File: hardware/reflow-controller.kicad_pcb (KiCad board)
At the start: 2 copper layers, 39.4 x 30.5 mm, 27 parts, among them J1 USB_B_Mini, J2 Conn_01x02, J3 Conn_02x03_Odd_Even, J4 Conn_01x02, J5 Conn_01x04, Q1 BC817, U1 MAX31855KASA, U2 AP2127K-3.3, U3 ATmega8U2-AU, Y1 8MHz

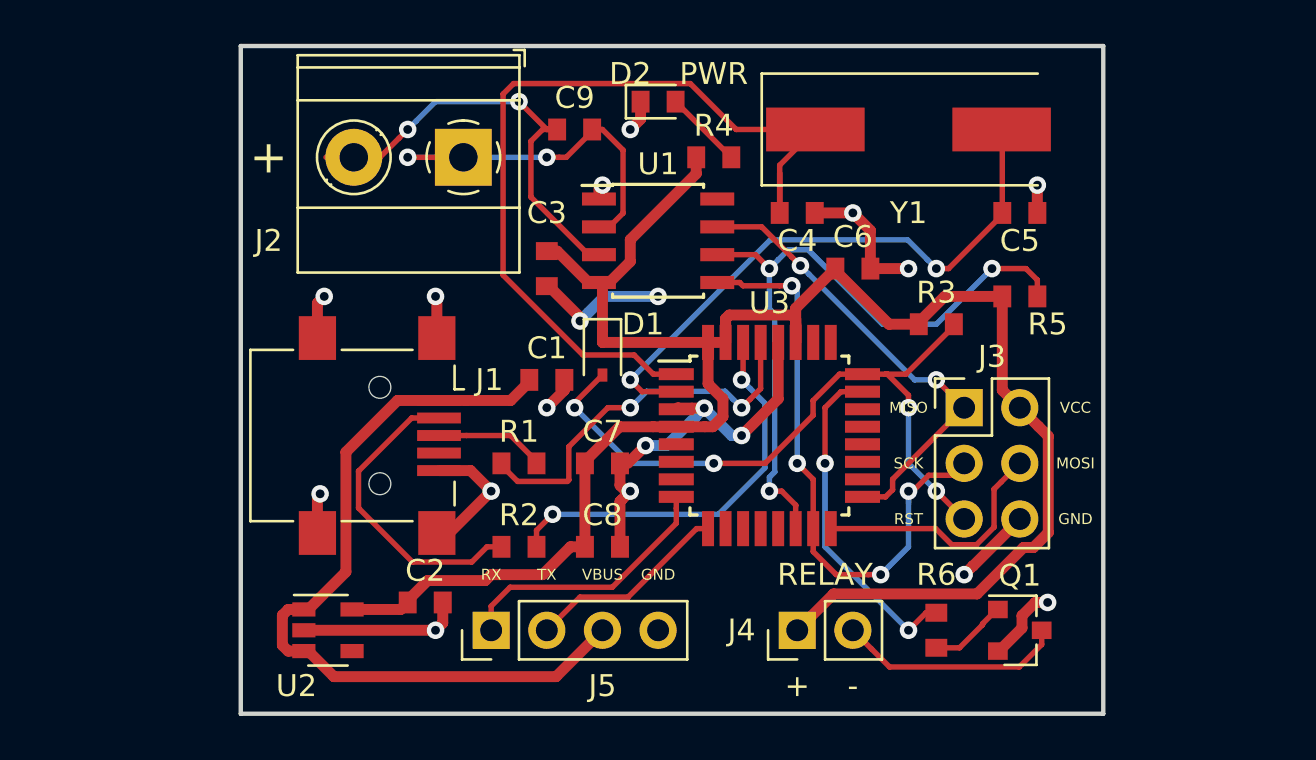
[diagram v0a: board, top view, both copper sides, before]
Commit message: Fixed power supply when programmed by ISP, added mounting holes, replaced mini USB connector with micro connector.
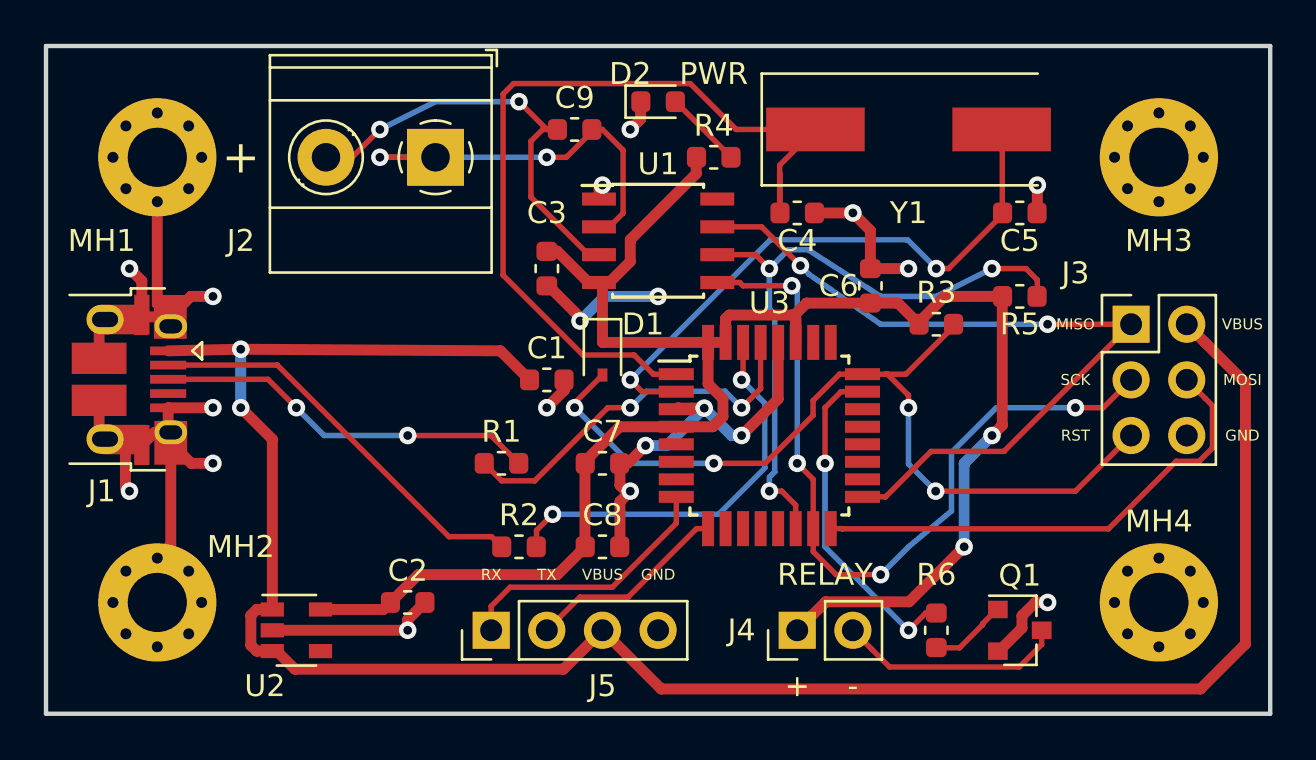
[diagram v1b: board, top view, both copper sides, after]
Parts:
- added MH1: MountingHole_Pad, MountingHole:MountingHole_2.7mm_M2.5_Pad_Via, F.Cu at (161.3, 52.1)
- added MH2: MountingHole_Pad, MountingHole:MountingHole_2.7mm_M2.5_Pad_Via, F.Cu at (161.3, 72.4)
- added MH3: MountingHole_Pad, MountingHole:MountingHole_2.7mm_M2.5_Pad_Via, F.Cu at (207.0, 52.1)
- added MH4: MountingHole_Pad, MountingHole:MountingHole_2.7mm_M2.5_Pad_Via, F.Cu at (207.0, 72.4)
- J1: value USB_B_Mini -> USB_B_Micro; footprint Connector_USB:USB_Mini-B_Lumberg_2486_01_Horizontal -> Connector_USB:USB_Micro-B_Amphenol_10103594-0001LF_Horizontal
- moved J1 11.7 mm to (160.0, 62.2)
- moved J3 8.52 mm to (205.7, 59.7)
- moved U2 1.44 mm to (167.6, 73.7)
- moved J2 1.27 mm to (174.0, 52.1)
- moved C6 1.12 mm to (193.8, 57.9), turned to 90 degrees
- moved C2 0.80 mm to (172.7, 72.4)
- moved R1 0.80 mm to (177.0, 66.0)
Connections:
- J3 pad 2: VCC -> /VBUS
- U2 pad 4: Net-(U2-Pad4) -> (no net)
- U3 pad 10: Net-(U3-Pad10) -> (no net)
- U3 pad 11: Net-(U3-Pad11) -> (no net)
- U3 pad 12: Net-(U3-Pad12) -> (no net)
- U3 pad 13: Net-(U3-Pad13) -> (no net)
- U3 pad 18: Net-(U3-Pad18) -> (no net)
- U3 pad 19: Net-(U3-Pad19) -> (no net)
- U3 pad 20: Net-(U3-Pad20) -> (no net)
- U3 pad 21: Net-(U3-Pad21) -> (no net)
- U3 pad 22: Net-(U3-Pad22) -> (no net)
- U3 pad 25: Net-(U3-Pad25) -> (no net)
- U3 pad 26: Net-(U3-Pad26) -> (no net)
- U3 pad 5: Net-(U3-Pad5) -> (no net)
- U3 pad 6: Net-(U3-Pad6) -> (no net)
- U3 pad 7: Net-(U3-Pad7) -> (no net)
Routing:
- net /VBUS: track 36.6 -> 96.2 mm, vias 0 -> 2
- net GND: track 62.4 -> 84.1 mm, vias 24 -> 19
- net /MISO: track 21.3 -> 36.0 mm
- net Net-(J1-Pad3): track 5.03 -> 17.6 mm, vias 0 -> 2
- net /MOSI: track 11.5 -> 22.6 mm
- net /SCK: track 28.2 -> 36.8 mm
- net /RST: track 31.7 -> 39.8 mm
- net Net-(J1-Pad2): track 14.2 -> 18.7 mm
- net VCC: track 91.9 -> 88.2 mm, vias 0 -> 2
- net Net-(C9-Pad2): track 16.3 -> 18.8 mm
- net /SS: track 32.0 -> 30.5 mm
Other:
- board size 39.4 x 30.5 mm -> 55.9 x 30.5 mm
- board text removed: "VCC"

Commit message: Fixed minimum values for solder mask clearance and width.
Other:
- rule pad_to_mask_clearance: 0.2 -> 0.0762
- rule solder_mask_min_width: 0.25 -> 0.1016
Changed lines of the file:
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@@
-(kicad_pcb (version 20171130) (host pcbnew 6.0.0-rc1-unknown-6a6d580~84~ubuntu18.04.1)
+(kicad_pcb (version 20171130) (host pcbnew 6.0.0-rc1-unknown-c4cd81a~84~ubuntu18.04.1)
   (general
     (thickness 1.6)
@@
     (pad_size 1.524 1.524)
     (pad_drill 0.762)
-    (pad_to_mask_clearance 0.2)
-    (solder_mask_min_width 0.25)
+    (pad_to_mask_clearance 0.0762)
+    (solder_mask_min_width 0.1016)
     (aux_axis_origin 0 0)
     (visible_elements FFFFFF7F)

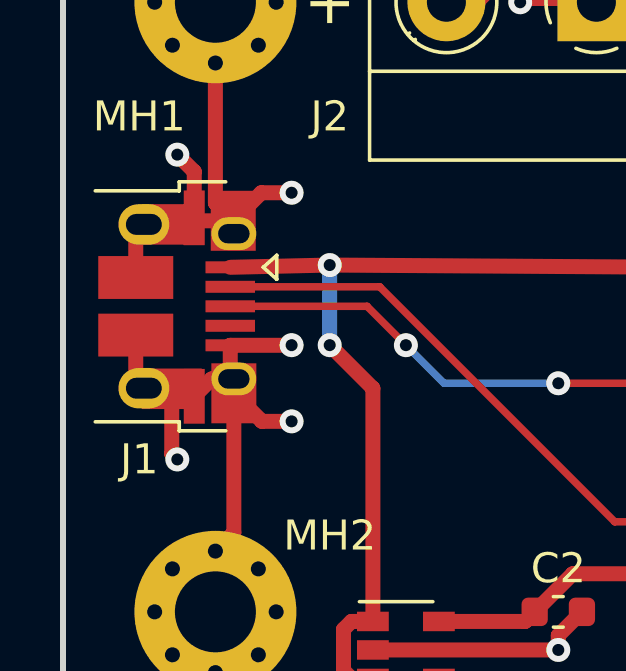
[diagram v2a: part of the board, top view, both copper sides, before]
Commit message: Adjusted solder mask relief and rewrote PC code in C++.
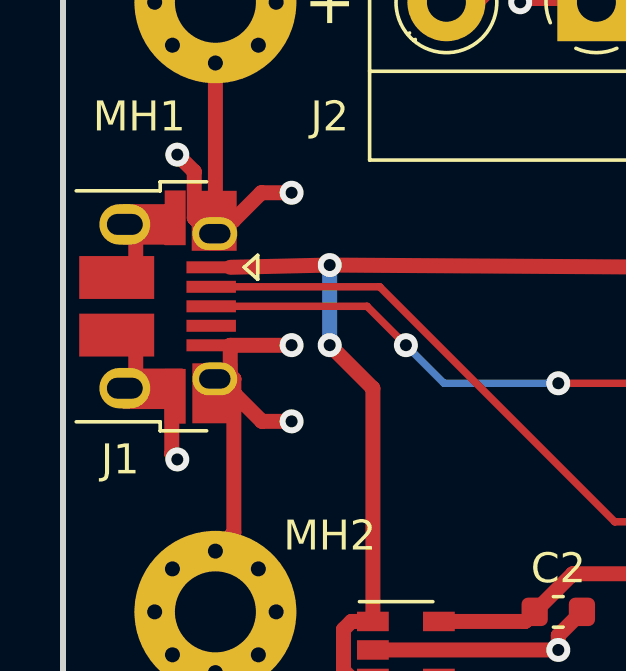
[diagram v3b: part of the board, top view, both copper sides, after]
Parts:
- moved J1 0.64 mm to (159.4, 62.2)
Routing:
- net GND: track 84.1 -> 83.3 mm
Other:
- rule pad_to_mask_clearance: 0.0762 -> 0.0508
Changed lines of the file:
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@@
-(kicad_pcb (version 20171130) (host pcbnew 6.0.0-rc1-unknown-c4cd81a~84~ubuntu18.04.1)
+(kicad_pcb (version 20171130) (host pcbnew 6.0.0-rc1-unknown-be0935b~84~ubuntu18.04.1)
   (general
     (thickness 1.6)
     (drawings 19)
-    (tracks 369)
+    (tracks 368)
     (zones 0)
     (modules 31)
@@
     (pad_size 1.524 1.524)
     (pad_drill 0.762)
-    (pad_to_mask_clearance 0.0762)
+    (pad_to_mask_clearance 0.0508)
     (solder_mask_min_width 0.1016)
     (aux_axis_origin 0 0)
@@
   )
   (module Connector_USB:USB_Micro-B_Amphenol_10103594-0001LF_Horizontal (layer F.Cu)
-    (at 160.02 62.23 270)
+    (at 159.385 62.23 270)
     (descr "Micro USB Type B 10103594-0001LF, http://cdn.amphenol-icc.com/media/wysiwyg/files/drawing/10103594.pdf")
     (tags "USB USB_B USB_micro USB_OTG")
@@
   (segment (start 161.785 64.505) (end 161.905 64.625) (width 0.5) (layer F.Cu) (net 1) (status 30))
   (segment (start 161.785 63.505) (end 161.785 64.505) (width 0.5) (layer F.Cu) (net 1) (status 30))
-  (segment (start 161.165 64.625) (end 160.585 65.205) (width 0.5) (layer F.Cu) (net 1) (status 30))
   (segment (start 161.905 64.625) (end 161.165 64.625) (width 0.5) (layer F.Cu) (net 1) (status 30))
   (segment (start 160.685 59.355) (end 160.585 59.255) (width 0.5) (layer F.Cu) (net 1) (status 30))
